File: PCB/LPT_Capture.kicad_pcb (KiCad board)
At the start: 2 copper layers, 36 x 20.8 mm, 12 parts, among them J1 USB3155-XX-X_REVA, J2 DB25 Male, U1 FT245RL

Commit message: add MPN to symbols, export fab_bom & centroid
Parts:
- added N1: DB25_backshell, 000_LOCAL:db25_backshell, F.Cu at (150.0, 90.2)
- added REF**: Fiducial_0.75mm_Mask1.5mm, 000_LOCAL:Fiducial_0.75mm_Mask1.5mm, F.Cu at (166.8, 107.2)
- added REF**: Fiducial_0.75mm_Mask1.5mm, 000_LOCAL:Fiducial_0.75mm_Mask1.5mm, F.Cu at (135.5, 97.5)
- added REF**: Fiducial_0.75mm_Mask1.5mm, 000_LOCAL:Fiducial_0.75mm_Mask1.5mm, F.Cu at (135.5, 109.8)
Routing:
- net GND: vias 16 -> 15

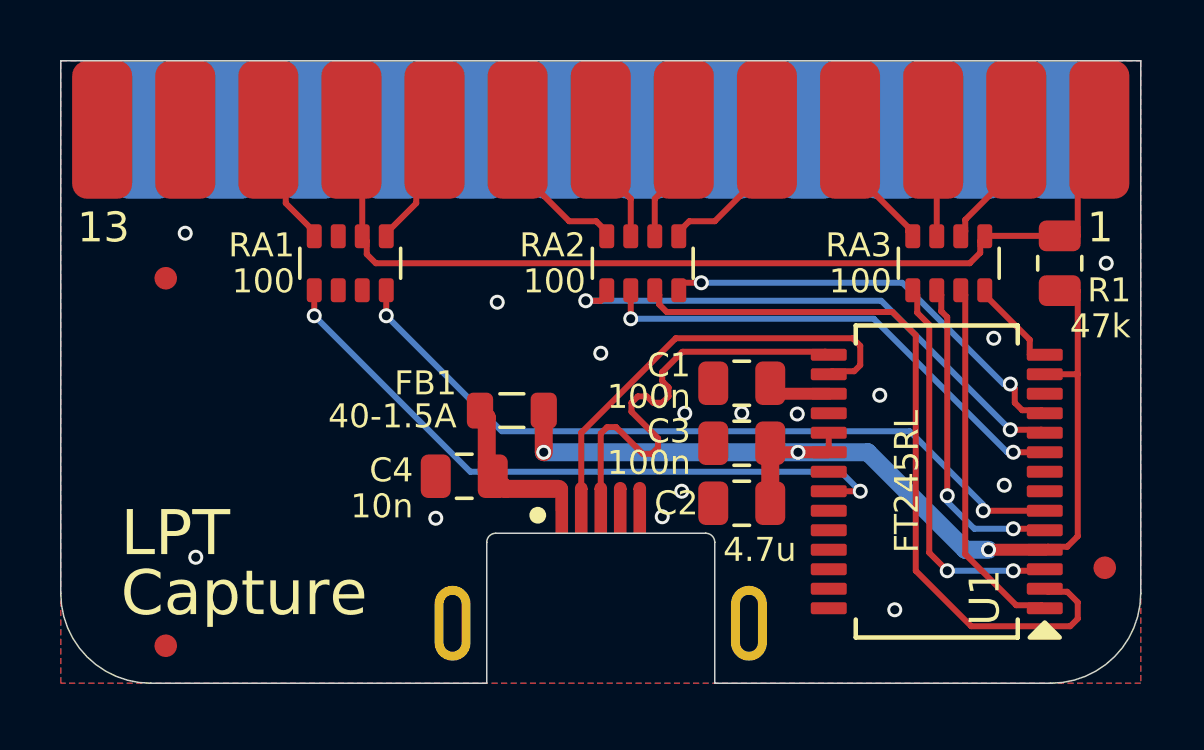
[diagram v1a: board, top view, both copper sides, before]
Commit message: double vias on power
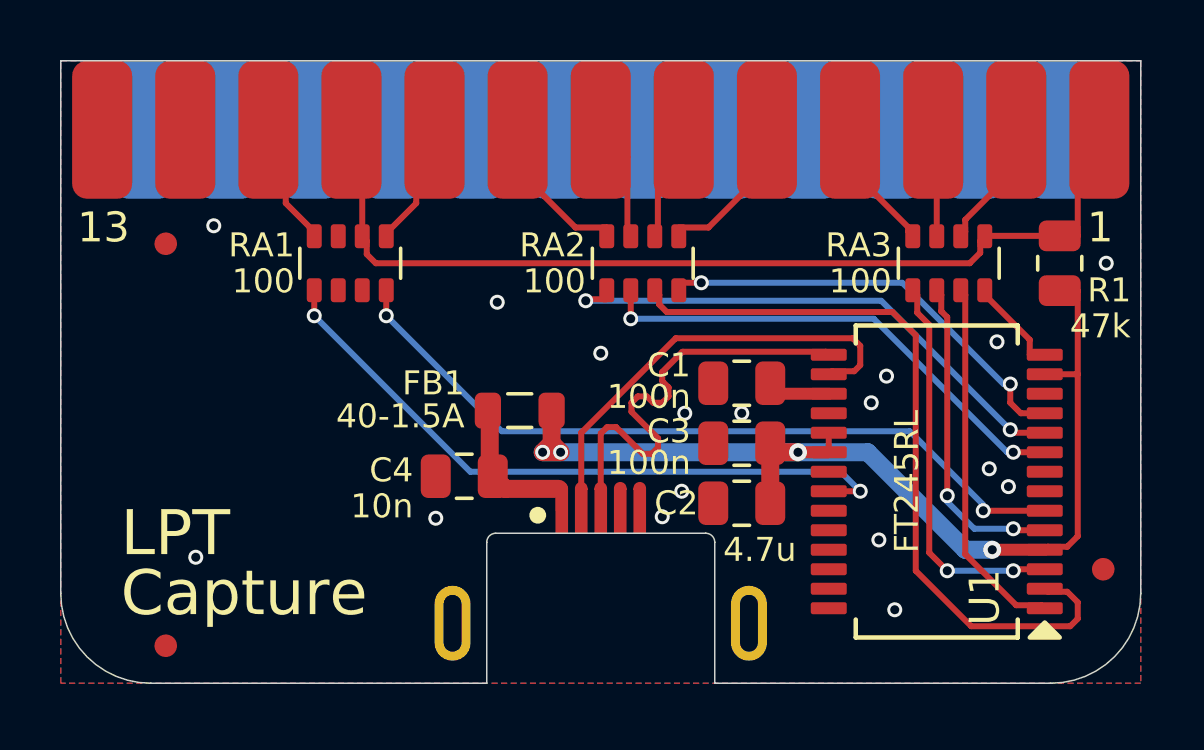
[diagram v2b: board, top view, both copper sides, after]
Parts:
- moved REF** 1.15 mm to (135.5, 96.3)
- moved FB1 0.26 mm to (147.3, 101.9)
- moved REF** 0.07 mm to (166.8, 107.2)
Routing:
- net VCC: track 35.4 -> 35.1 mm, vias 3 -> 4
- net GND: vias 15 -> 17

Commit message: update eol FT245R to FT245RN
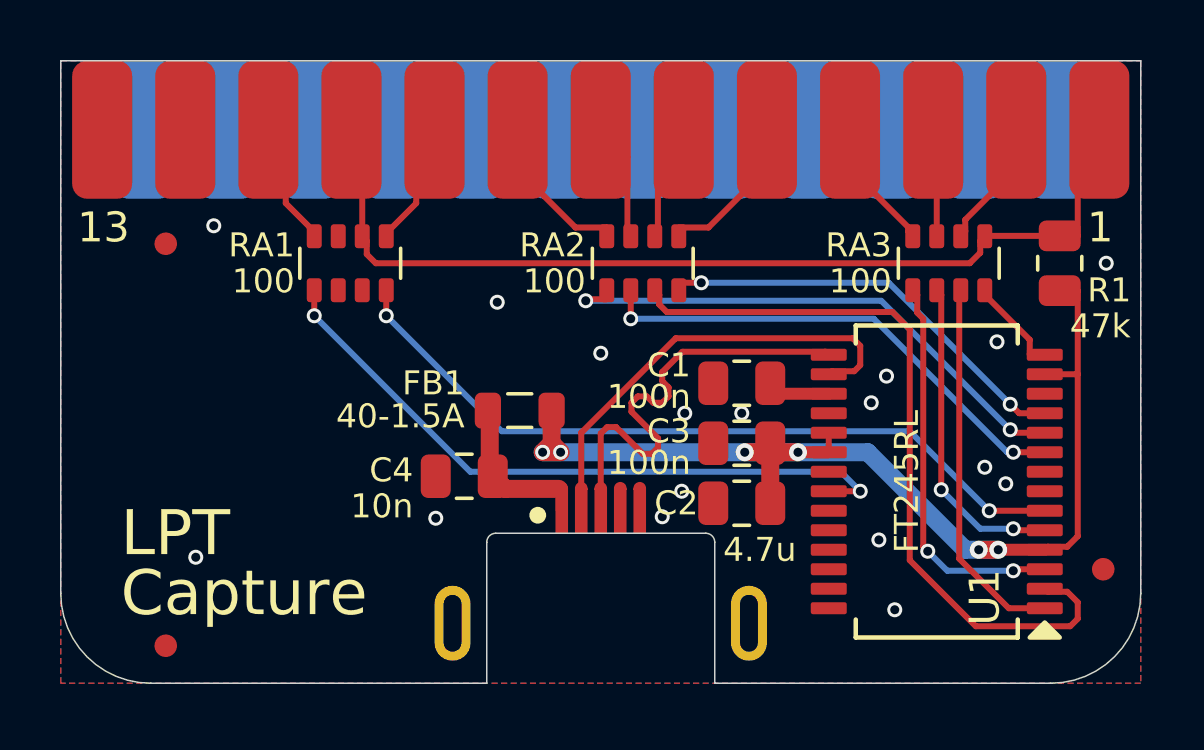
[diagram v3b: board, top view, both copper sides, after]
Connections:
- J2 pad 13: unconnected-(J2-Pad13) -> /ONLINE
- J2 pad 14: unconnected-(J2-P14-Pad14) -> /~{AUTOFD}
- J2 pad 17: unconnected-(J2-P17-Pad17) -> /~{SELIN}
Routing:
- net VCC: track 35.1 -> 36.5 mm, vias 4 -> 6

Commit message: component library & models
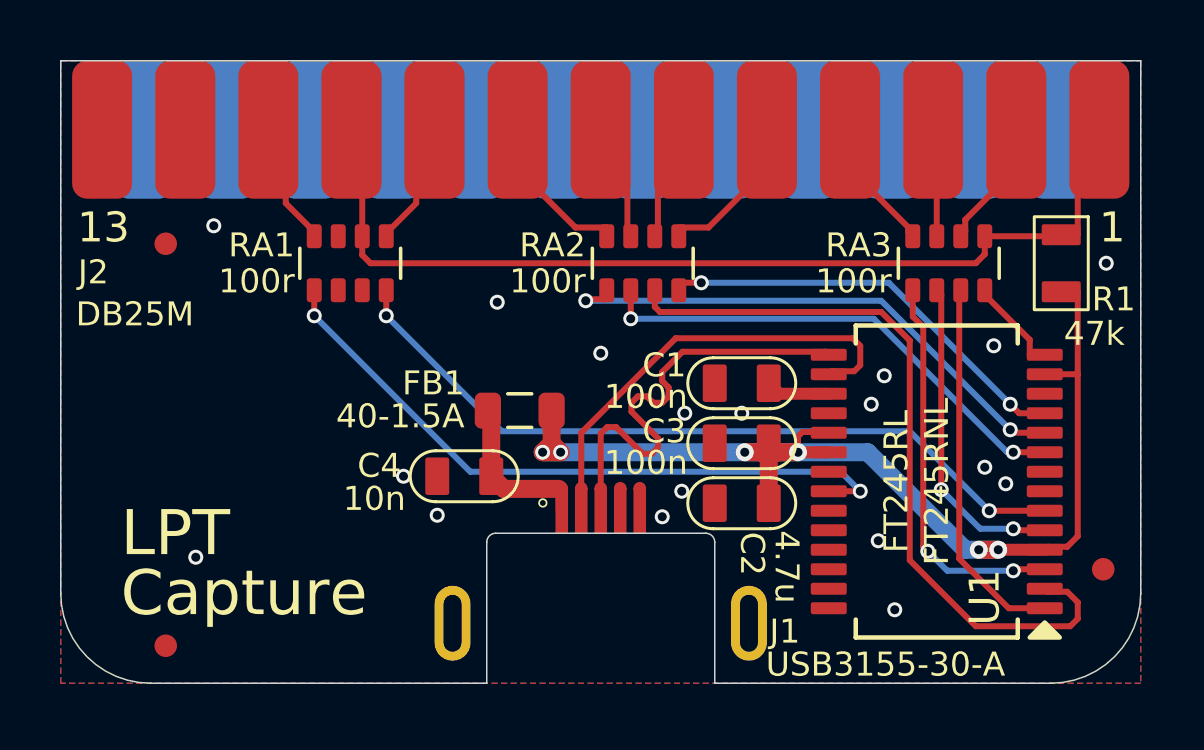
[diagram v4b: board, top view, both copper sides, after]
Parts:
- J1: value USB3155-XX-X_REVA -> USB3155-30-A; footprint 000_LOCAL:GCT_USB3155-XX-X_REVA -> 000_LOCAL:GCT_USB3155-XX-X
- J2: value DB25 Male -> DB25M
- N1: footprint 000_LOCAL:db25_backshell -> 000_LOCAL:DSUB-25_Housing
- RA1, RA2, RA3: value 100 -> 100r
- REF** (x3): value Fiducial_0.75mm_Mask1.5mm -> Fiducial; footprint 000_LOCAL:Fiducial_0.75mm_Mask1.5mm -> 000_LOCAL:Fiducial_0.75_1.5
- moved N1 2.30 mm to (150.0, 92.5), turned to 180 degrees
- moved J2 1.90 mm to (150.0, 90.1)
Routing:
- net VCC: track 36.5 -> 37.3 mm
- net GND: vias 17 -> 18
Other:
- board text added: "FT245RNL"

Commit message: cleanup symb & footp libs, add ONLINE
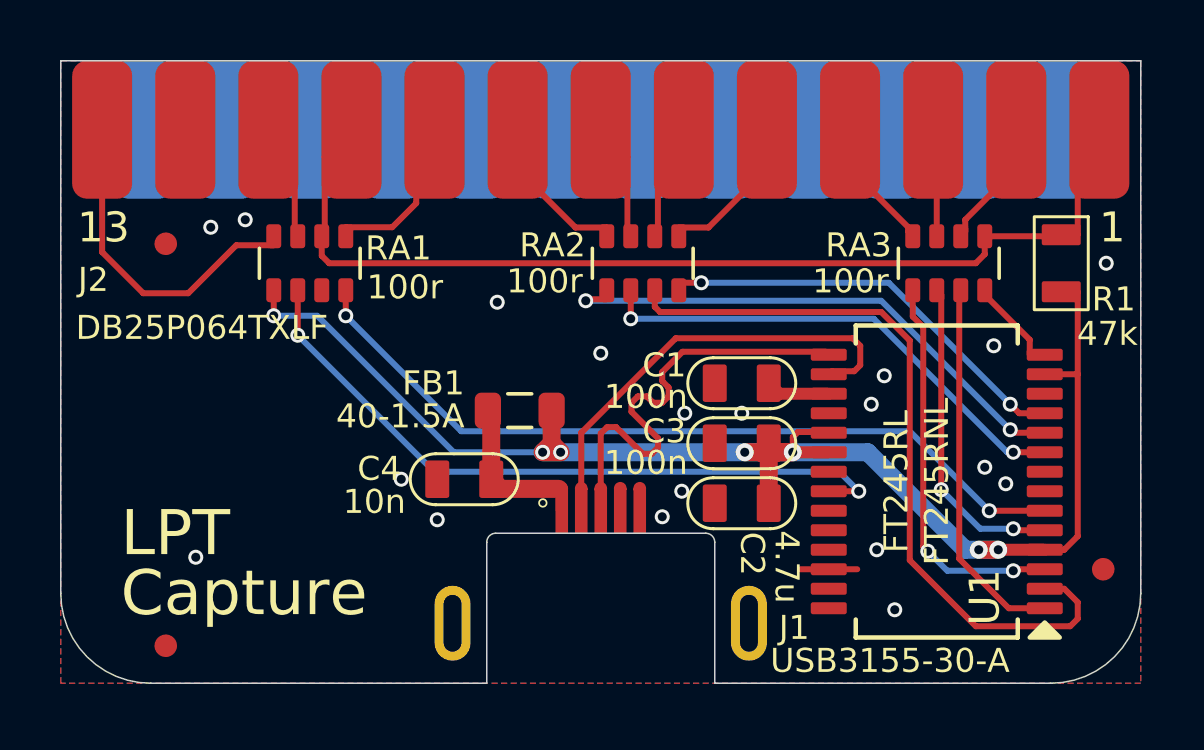
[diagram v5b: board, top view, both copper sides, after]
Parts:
- J1: footprint 000_LOCAL:GCT_USB3155-XX-X -> 000_LOCAL:USB3155-xx-x
- J2: value DB25M -> DB25P064TXLF
- N1: value DB25_backshell -> 956-025-010R031
- moved RA1 1.35 mm to (140.3, 97.0)
- moved C4 0.10 mm to (145.4, 104.2)
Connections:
- RA1 pad 1: /~{TXE} -> VCC
- RA1 pad 2: unconnected-(RA1-R2.1-Pad2) -> /~{TXE}
- RA1 pad 7: unconnected-(RA1-R2.2-Pad7) -> /BUSY
- RA1 pad 8: /BUSY -> /ONLINE
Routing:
- net VCC: track 37.3 -> 49.6 mm, vias 6 -> 7
- net /ONLINE: track 0.00 -> 11.3 mm
- net GND: track 0.00 -> 1.90 mm, vias 18 -> 19
- net /~{STROBE}: track 32.8 -> 34.5 mm
- net /PD7: track 4.22 -> 5.68 mm
- net /D7: track 25.6 -> 26.9 mm
- net /~{TXE}: track 22.5 -> 23.4 mm
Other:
- board text added: "BACKSHELL: ${1bfda150-39ff-4566-b43c-ab5bdfed869d:VALUE}"

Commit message: strobe>ack via unused 100r
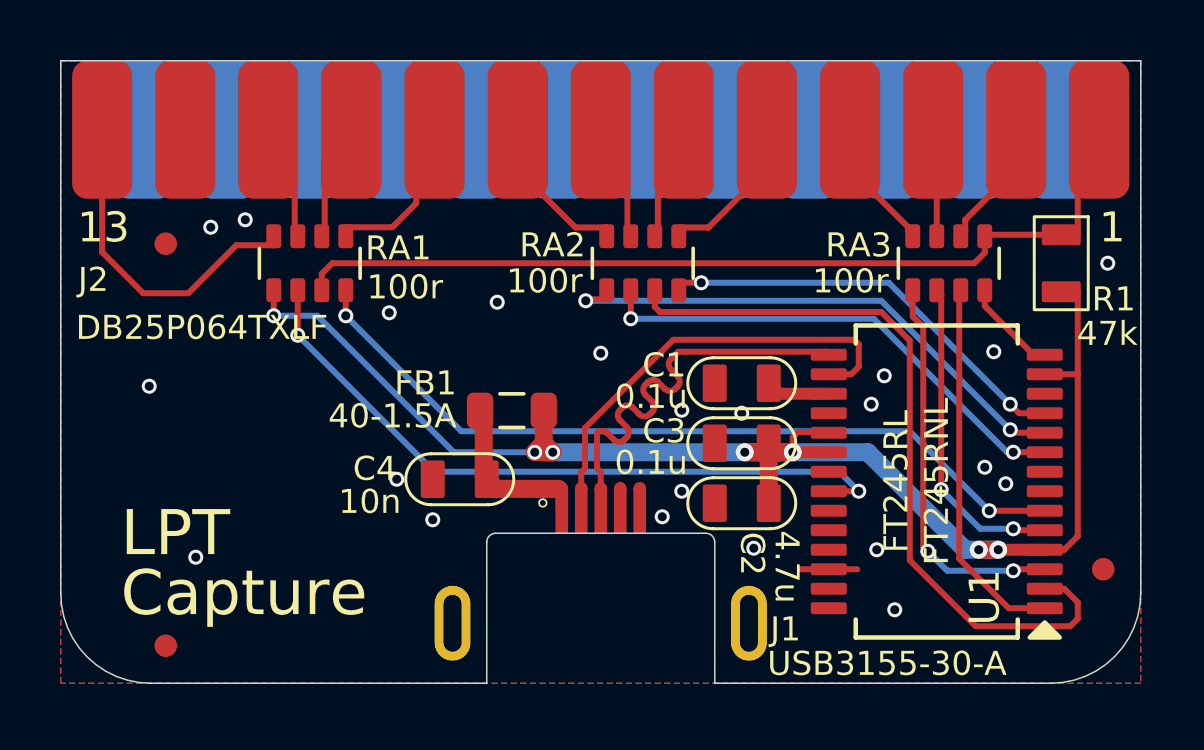
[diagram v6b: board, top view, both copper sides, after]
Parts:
- C1, C3: value 100n -> 0.1u
- moved FB1 0.26 mm to (147.0, 101.9)
- moved C4 0.15 mm to (145.3, 104.2)
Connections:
- net /~{RST_ERR} renamed /~{RESET}
- J2 pad 10: /~{STROBE} -> /~{ACK}
- RA1 pad 3: unconnected-(RA1-R3.1-Pad3) -> /~{STROBE}
- RA1 pad 6: /~{STROBE} -> /~{ACK}
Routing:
- net /~{STROBE}: track 34.5 -> 30.4 mm
- net /~{ACK}: track 0.00 -> 3.96 mm
- net GND: vias 19 -> 22
